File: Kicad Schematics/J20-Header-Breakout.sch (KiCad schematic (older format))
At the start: 1 part, among them P301 CONN_02X20

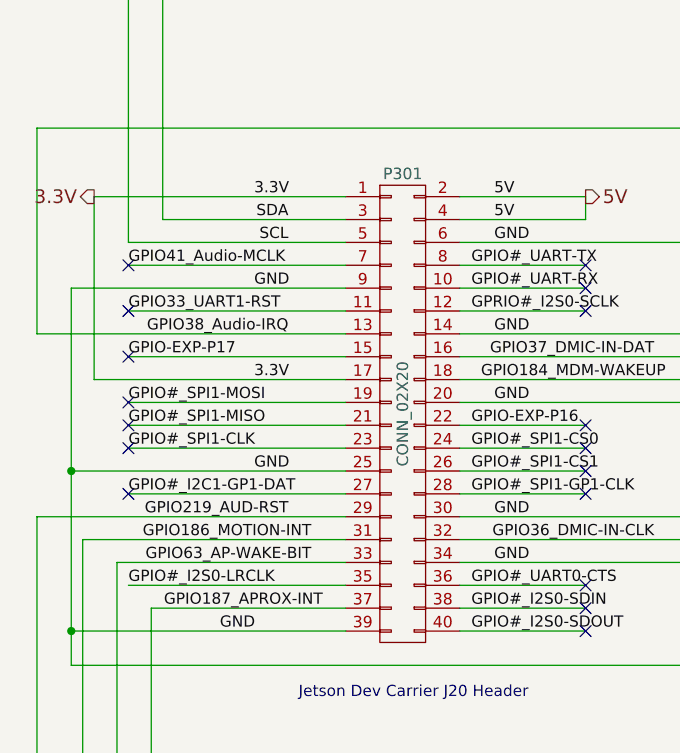
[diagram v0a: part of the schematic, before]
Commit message: Reduced number of components
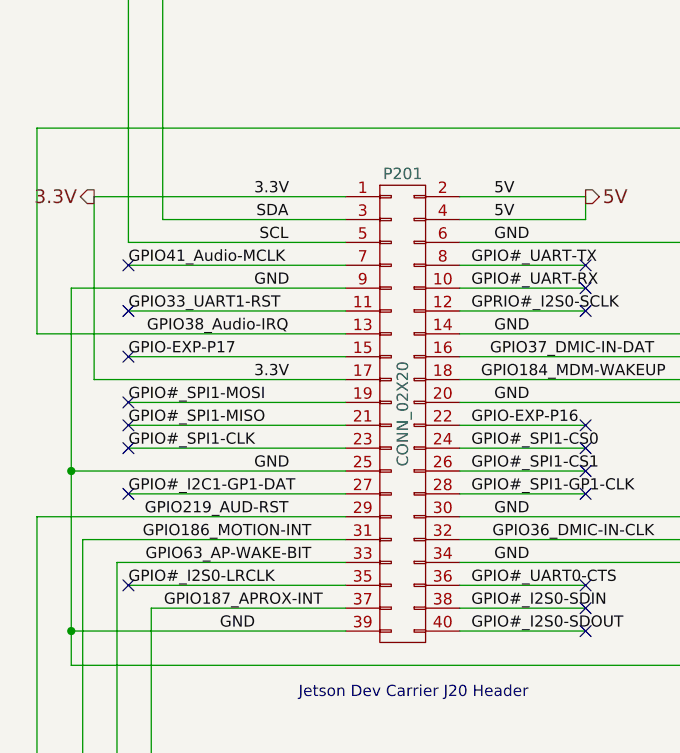
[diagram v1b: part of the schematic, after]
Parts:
- P201: renamed from P301; footprint Pin_Headers:Pin_Header_Straight_2x20_Pitch2.54mm -> Socket_Strips:Socket_Strip_Straight_2x20_Pitch2.54mm
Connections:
- no-connect marks 17 -> 18
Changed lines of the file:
@@
 $Descr A4 11693 8268
 encoding utf-8
-Sheet 3 5
+Sheet 2 4
 Title "GPIO Breakout"
 Date "2017-03-17"
@@
 $EndDescr
 $Comp
-L CONN_02X20 P301
+L CONN_02X20 P201
 U 1 1 58CAB084
 P 4650 4000
-F 0 "P301" H 4650 5050 50  0000 C CNN
+F 0 "P201" H 4650 5050 50  0000 C CNN
 F 1 "CONN_02X20" V 4650 4000 50  0000 C CNN
-F 2 "Pin_Headers:Pin_Header_Straight_2x20_Pitch2.54mm" H 4650 3050 50  0001 C CNN
+F 2 "Socket_Strips:Socket_Strip_Straight_2x20_Pitch2.54mm" H 4650 3050 50  0001 C CNN
 F 3 "" H 4650 3050 50  0000 C CNN
 	1    4650 4000
@@
 NoConn ~ 5450 4850
 NoConn ~ 5450 4950
+NoConn ~ 3450 4750
 $EndSCHEMATC

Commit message: Layout Done
Minor Tweaks were made to Schematic
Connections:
- no-connect marks 18 -> 20
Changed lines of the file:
@@
 	3450 4150 4400 4150
 Wire Wire Line
-	3200 4250 4400 4250
+	3350 4250 4400 4250
 Wire Wire Line
 	3450 4350 4400 4350
@@
 GPIO#_I2S0-SDOUT
 Wire Wire Line
-	6100 3250 6100 5100
+	6100 5100 6100 3250
 Connection ~ 6100 3650
 Connection ~ 6100 3950
@@
 Wire Wire Line
 	5450 3150 5450 3050
-Wire Wire Line
-	3300 3850 4400 3850
-Wire Wire Line
-	3300 3850 3300 3050
 Text HLabel 5450 3050 2    60   Output ~ 0
 5V
@@
 NoConn ~ 5450 4950
 NoConn ~ 3450 4750
+NoConn ~ 3350 4250
+Wire Wire Line
+	3400 3850 4400 3850
+NoConn ~ 3400 3850
+$Comp
+L GND #PWR01
+U 1 1 58EF32BF
+P 5650 5150
+F 0 "#PWR01" H 5650 4900 50  0001 C CNN
+F 1 "GND" H 5650 5000 50  0000 C CNN
+F 2 "" H 5650 5150 50  0000 C CNN
+F 3 "" H 5650 5150 50  0000 C CNN
+	1    5650 5150
+	1    0    0    -1
+$EndComp
+Wire Wire Line
+	5650 5150 5650 5100
+Connection ~ 5650 5100
 $EndSCHEMATC

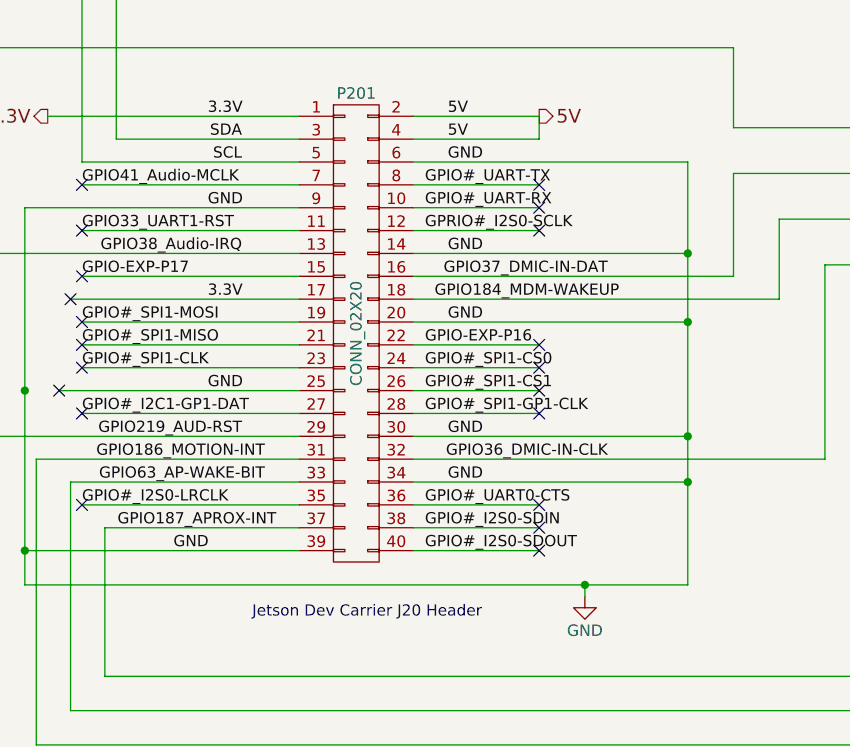
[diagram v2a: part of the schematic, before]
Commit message: Redesign - Rev B Board
Smaller Board, more symmetric, will be more stable
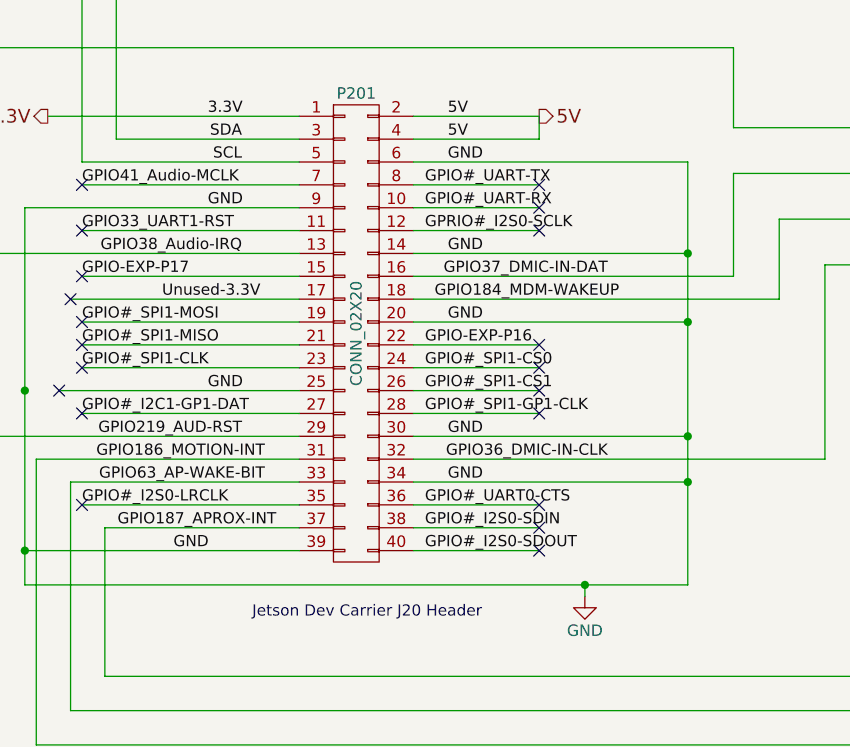
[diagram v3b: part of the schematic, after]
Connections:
- net 3.3V: no longer P201.17 (P17)
- new net Unused-3.3V: P201.17 (P17)
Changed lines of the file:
@@
 Text Label 3450 4350 0    49   ~ 0
 GPIO#_I2C1-GP1-DAT
-Text Label 4000 3850 0    49   ~ 0
-3.3V
+Text Label 3800 3850 0    49   ~ 0
+Unused-3.3V
 Text Label 3450 4750 0    49   ~ 0
 GPIO#_I2S0-LRCLK
@@
 GPIO#_I2S0-SDOUT
 Wire Wire Line
-	6100 5100 6100 3250
+	6100 3250 6100 5100
 Connection ~ 6100 3650
 Connection ~ 6100 3950
